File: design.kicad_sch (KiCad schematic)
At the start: 32 parts, among them J1 USB_A, J2 HRO_TYPE-C-31-M-12, J3 USB_A, SW1 EN, SW2 IO9, U1 AP22804AW5, U2 AP22804AW5, U3 ESP32-C3-WROOM-02-N4

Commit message: Update design.kicad_sch
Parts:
- gave numbers to parts that had none: 3
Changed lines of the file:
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@@
   (symbol (lib_id "power:+3.3V") (at 244.475 128.27 0) (unit 1)
     (in_bom yes) (on_board yes) (fields_autoplaced)
-    (property "Reference" "#PWR?" (id 0) (at 244.475 132.08 0)
+    (property "Reference" "#PWR0126" (id 0) (at 244.475 132.08 0)
       (effects (font (size 1.27 1.27)) hide)
     )
@@
   (symbol (lib_id "Device:C_Small") (at 237.49 133.985 0) (unit 1)
     (in_bom yes) (on_board yes)
-    (property "Reference" "C?" (id 0) (at 239.395 132.715 0)
+    (property "Reference" "C13" (id 0) (at 239.395 132.715 0)
       (effects (font (size 1.27 1.27)) (justify left))
     )
@@
   (symbol (lib_id "Regulator_Linear:MCP1700-3302E_SOT23") (at 226.06 128.27 0) (unit 1)
     (in_bom yes) (on_board yes)
-    (property "Reference" "U?" (id 0) (at 226.06 121.285 0))
+    (property "Reference" "U4" (id 0) (at 226.06 121.285 0))
     (property "Value" "MCP1700T-3302E" (id 1) (at 226.06 123.825 0))
     (property "Footprint" "Package_TO_SOT_SMD:SOT-23" (id 2) (at 226.06 122.555 0)
@@
   (symbol (lib_id "Device:C_Small") (at 213.36 133.985 0) (unit 1)
     (in_bom yes) (on_board yes)
-    (property "Reference" "C?" (id 0) (at 215.9 132.715 0)
+    (property "Reference" "C12" (id 0) (at 215.9 132.715 0)
       (effects (font (size 1.27 1.27)) (justify left))
     )
@@
   (symbol (lib_id "power:GND") (at 237.49 140.97 0) (unit 1)
     (in_bom yes) (on_board yes) (fields_autoplaced)
-    (property "Reference" "#PWR?" (id 0) (at 237.49 147.32 0)
+    (property "Reference" "#PWR0125" (id 0) (at 237.49 147.32 0)
       (effects (font (size 1.27 1.27)) hide)
     )
@@
   (symbol (lib_id "power:VCC") (at 207.01 128.27 0) (unit 1)
     (in_bom yes) (on_board yes) (fields_autoplaced)
-    (property "Reference" "#PWR?" (id 0) (at 207.01 132.08 0)
+    (property "Reference" "#PWR0124" (id 0) (at 207.01 132.08 0)
       (effects (font (size 1.27 1.27)) hide)
     )
@@
       (reference "#PWR0123") (unit 1) (value "GND") (footprint "")
     )
+    (path "/ff60fb19-afa6-4094-aadb-2fbb7283cdc9"
+      (reference "#PWR0124") (unit 1) (value "VCC") (footprint "")
+    )
+    (path "/e48e62da-a82e-4af6-87a5-4856bf756a8f"
+      (reference "#PWR0125") (unit 1) (value "GND") (footprint "")
+    )
     (path "/10960125-f5d3-4f7c-8b77-9cd9124e6ca3"
-      (reference "#PWR?") (unit 1) (value "+3.3V") (footprint "")
-    )
-    (path "/e48e62da-a82e-4af6-87a5-4856bf756a8f"
-      (reference "#PWR?") (unit 1) (value "GND") (footprint "")
-    )
-    (path "/ff60fb19-afa6-4094-aadb-2fbb7283cdc9"
-      (reference "#PWR?") (unit 1) (value "VCC") (footprint "")
+      (reference "#PWR0126") (unit 1) (value "+3.3V") (footprint "")
     )
     (path "/f840b762-87cb-4a72-9780-ad2fe364c8c2"
@@
       (reference "C11") (unit 1) (value "1uF") (footprint "Capacitor_SMD:C_0805_2012Metric")
     )
+    (path "/c44c2db8-4ba0-4612-a365-cdf0c217b601"
+      (reference "C12") (unit 1) (value "1uF") (footprint "Capacitor_SMD:C_0805_2012Metric")
+    )
     (path "/52f2afaf-d838-4cf3-b173-2a3c422559ac"
-      (reference "C?") (unit 1) (value "1uF") (footprint "Capacitor_SMD:C_0805_2012Metric")
-    )
-    (path "/c44c2db8-4ba0-4612-a365-cdf0c217b601"
-      (reference "C?") (unit 1) (value "1uF") (footprint "Capacitor_SMD:C_0805_2012Metric")
+      (reference "C13") (unit 1) (value "1uF") (footprint "Capacitor_SMD:C_0805_2012Metric")
     )
     (path "/84f91f18-93b9-4640-b399-413cf4103af7"
@@
     )
     (path "/ad0d0798-3677-4868-b360-d7f8762b6e0c"
-      (reference "U?") (unit 1) (value "MCP1700T-3302E") (footprint "Package_TO_SOT_SMD:SOT-23")
-    )
-  )
+      (reference "U4") (unit 1) (value "MCP1700T-3302E") (footprint "Package_TO_SOT_SMD:SOT-23")
+    )
+  )

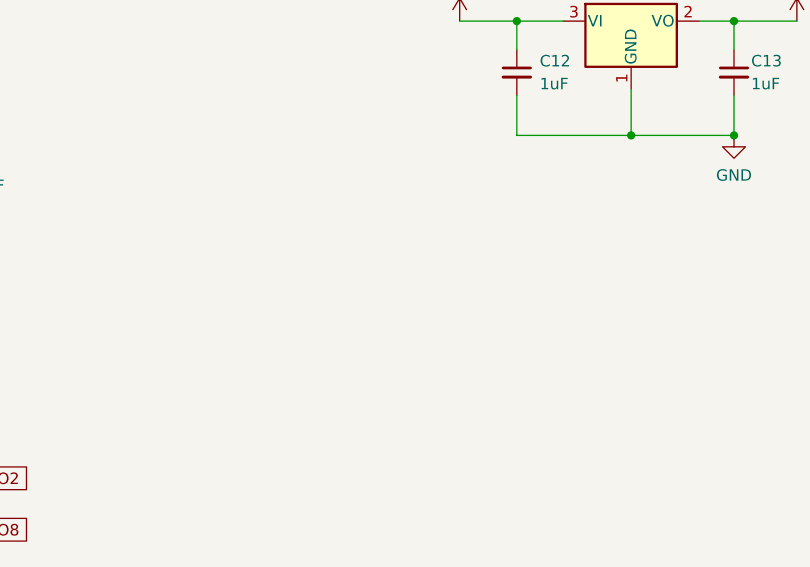
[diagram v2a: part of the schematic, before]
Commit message: add back variables for CI, rounded corners, mounting holes
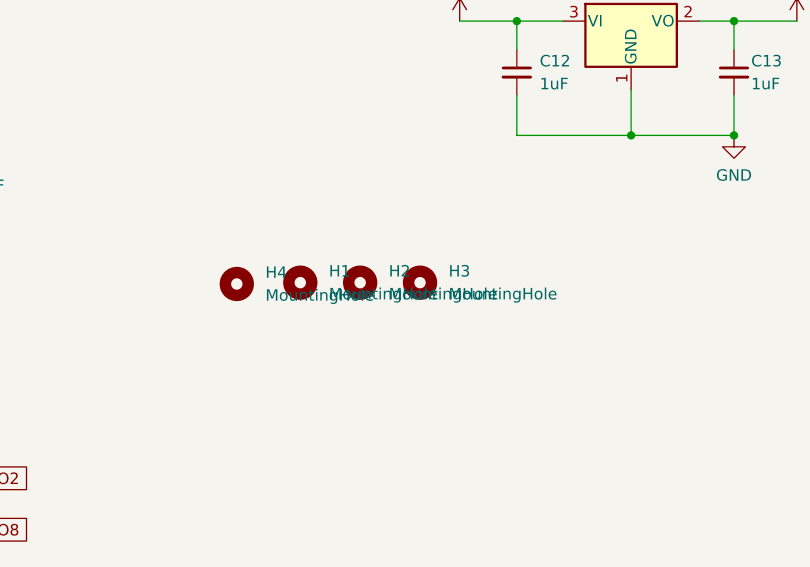
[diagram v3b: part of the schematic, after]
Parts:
- added H1, H2, H3, H4: MountingHole, MountingHole:MountingHole_2.7mm_M2.5_Pad_Via, symbol Mechanical:MountingHole
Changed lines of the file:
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@@
     (pin "1")
+  )
+  (symbol (lib_id "Mechanical:MountingHole") (at 195.952 157.3327 0) (unit 1)
+    (in_bom yes) (on_board yes) (fields_autoplaced)
+    (property "Reference" "H2" (id 0) (at 199.127 156.0626 0)
+      (effects (font (size 1.27 1.27)) (justify left))
+    )
+    (property "Value" "MountingHole" (id 1) (at 199.127 158.6026 0)
+      (effects (font (size 1.27 1.27)) (justify left))
+    )
+    (property "Footprint" "MountingHole:MountingHole_2.7mm_M2.5_Pad_Via" (id 2) (at 195.952 157.3327 0)
+      (effects (font (size 1.27 1.27)) hide)
+    )
+    (property "Datasheet" "~" (id 3) (at 195.952 157.3327 0)
+      (effects (font (size 1.27 1.27)) hide)
+    )
   )
   (symbol (lib_id "power:+3.3V") (at 244.475 128.27 0) (unit 1)
@@
     )
     (pin "1")
+  )
+  (symbol (lib_id "Mechanical:MountingHole") (at 202.604 157.3327 0) (unit 1)
+    (in_bom yes) (on_board yes) (fields_autoplaced)
+    (property "Reference" "H3" (id 0) (at 205.779 156.0626 0)
+      (effects (font (size 1.27 1.27)) (justify left))
+    )
+    (property "Value" "MountingHole" (id 1) (at 205.779 158.6026 0)
+      (effects (font (size 1.27 1.27)) (justify left))
+    )
+    (property "Footprint" "MountingHole:MountingHole_2.7mm_M2.5_Pad_Via" (id 2) (at 202.604 157.3327 0)
+      (effects (font (size 1.27 1.27)) hide)
+    )
+    (property "Datasheet" "~" (id 3) (at 202.604 157.3327 0)
+      (effects (font (size 1.27 1.27)) hide)
+    )
   )
   (symbol (lib_id "power:GND") (at 84.963 55.88 0) (unit 1)
@@
     (pin "1")
     (pin "2")
+  )
+  (symbol (lib_id "Mechanical:MountingHole") (at 189.3 157.3327 0) (unit 1)
+    (in_bom yes) (on_board yes) (fields_autoplaced)
+    (property "Reference" "H1" (id 0) (at 192.475 156.0626 0)
+      (effects (font (size 1.27 1.27)) (justify left))
+    )
+    (property "Value" "MountingHole" (id 1) (at 192.475 158.6026 0)
+      (effects (font (size 1.27 1.27)) (justify left))
+    )
+    (property "Footprint" "MountingHole:MountingHole_2.7mm_M2.5_Pad_Via" (id 2) (at 189.3 157.3327 0)
+      (effects (font (size 1.27 1.27)) hide)
+    )
+    (property "Datasheet" "~" (id 3) (at 189.3 157.3327 0)
+      (effects (font (size 1.27 1.27)) hide)
+    )
   )
   (symbol (lib_id "Device:R_Small") (at 62.23 172.72 0) (unit 1)
@@
     (pin "1")
     (pin "2")
+  )
+  (symbol (lib_id "Mechanical:MountingHole") (at 182.245 157.48 0) (unit 1)
+    (in_bom yes) (on_board yes) (fields_autoplaced)
+    (property "Reference" "H4" (id 0) (at 185.42 156.2099 0)
+      (effects (font (size 1.27 1.27)) (justify left))
+    )
+    (property "Value" "MountingHole" (id 1) (at 185.42 158.7499 0)
+      (effects (font (size 1.27 1.27)) (justify left))
+    )
+    (property "Footprint" "MountingHole:MountingHole_2.7mm_M2.5_Pad_Via" (id 2) (at 182.245 157.48 0)
+      (effects (font (size 1.27 1.27)) hide)
+    )
+    (property "Datasheet" "~" (id 3) (at 182.245 157.48 0)
+      (effects (font (size 1.27 1.27)) hide)
+    )
   )
   (symbol (lib_id "power:+3.3V") (at 147.955 168.275 0) (unit 1)
@@
       (reference "C13") (unit 1) (value "1uF") (footprint "Capacitor_SMD:C_0805_2012Metric")
     )
+    (path "/5f301e7a-86a4-4795-8d32-72efdf0b2bb9"
+      (reference "H1") (unit 1) (value "MountingHole") (footprint "MountingHole:MountingHole_2.7mm_M2.5_Pad_Via")
+    )
+    (path "/04f2b487-a681-4972-a368-4090dc0379f6"
+      (reference "H2") (unit 1) (value "MountingHole") (footprint "MountingHole:MountingHole_2.7mm_M2.5_Pad_Via")
+    )
+    (path "/2debdc1e-400e-4c02-b127-99d5f4c11c82"
+      (reference "H3") (unit 1) (value "MountingHole") (footprint "MountingHole:MountingHole_2.7mm_M2.5_Pad_Via")
+    )
+    (path "/96dd7c86-f7f4-4e0a-8949-254cf6044732"
+      (reference "H4") (unit 1) (value "MountingHole") (footprint "MountingHole:MountingHole_2.7mm_M2.5_Pad_Via")
+    )
     (path "/84f91f18-93b9-4640-b399-413cf4103af7"
